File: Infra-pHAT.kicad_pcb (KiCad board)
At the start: 2 copper layers, 64 x 30 mm, 24 parts, among them Q1 BC817, U1 CAT24C32WI-GT3

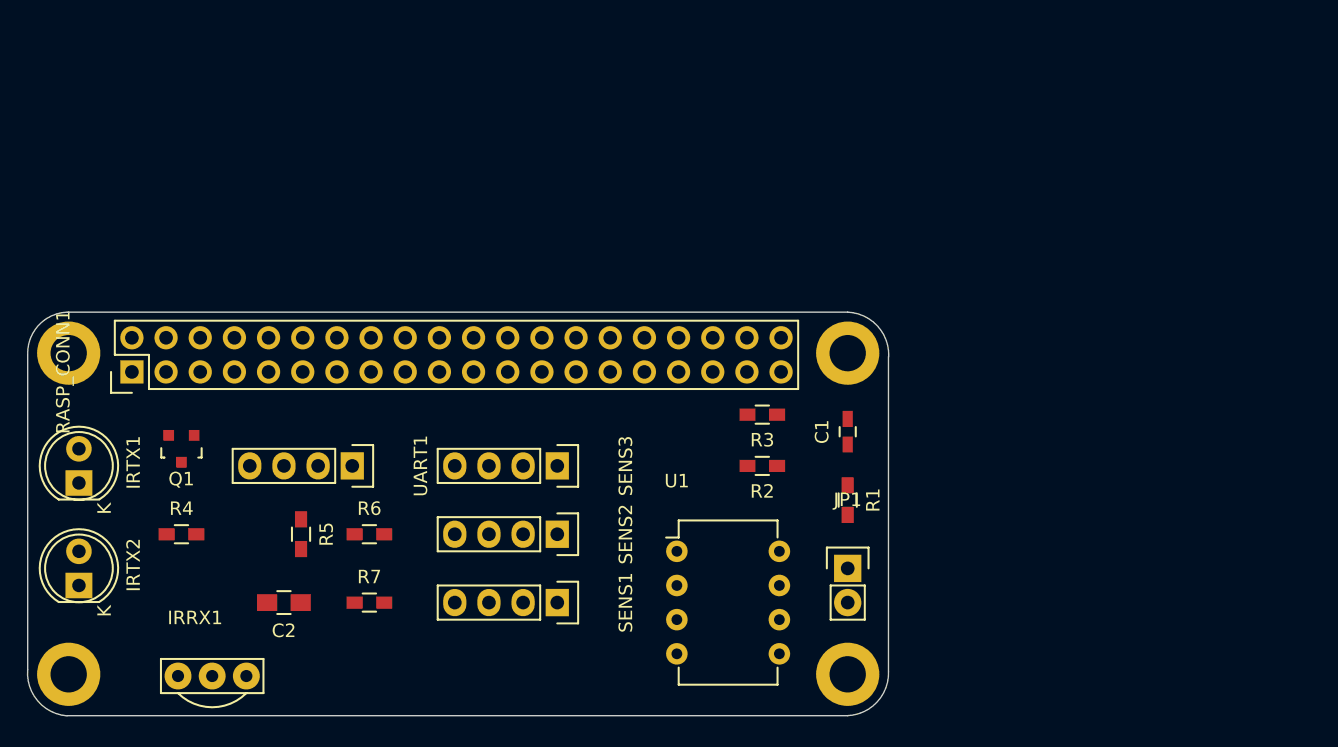
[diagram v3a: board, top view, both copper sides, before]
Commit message: Infra-pHAT.kicad_pcb: Fix edge cuts
Signed-off-by: Leon Anavi <leon@anavi.org>
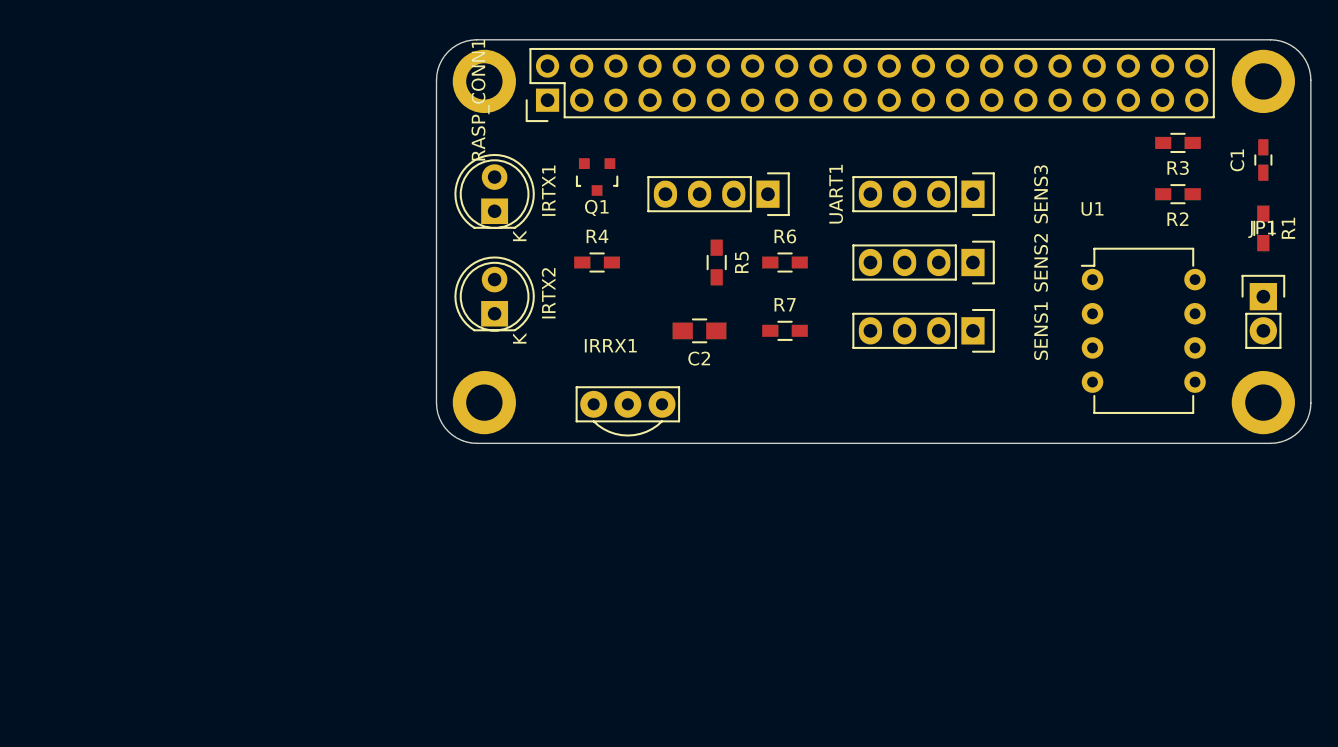
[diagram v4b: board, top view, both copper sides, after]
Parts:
- moved C1 36.9 mm to (210.0, 83.9)
- moved C2 36.9 mm to (168.1, 96.6)
- moved JP1 36.9 mm to (210.0, 94.1)
- moved Q1 36.9 mm to (160.4, 85.2)
- moved R1 36.9 mm to (210.0, 89.0)
- moved R2 36.9 mm to (203.6, 86.5)
- moved R3 36.9 mm to (203.6, 82.7)
- moved R4 36.9 mm to (160.4, 91.6)
- moved R5 36.9 mm to (169.3, 91.6)
- moved R6 36.9 mm to (174.4, 91.6)
- moved R7 36.9 mm to (174.4, 96.6)
- moved REF2 36.9 mm to (210.0, 78.1)
- moved REF3 36.9 mm to (210.0, 102.0)
- moved SENS1 36.9 mm to (188.4, 96.6)
- moved SENS2 36.9 mm to (188.4, 91.6)
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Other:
- board size 64 x 30 mm -> 65 x 30 mm
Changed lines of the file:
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@@
     (links 59)
     (no_connects 59)
-    (area 105.975429 93.919 194.252572 128.149)
+    (area 105.975429 74.953599 213.551101 126.653)
     (thickness 1.6)
-    (drawings 8)
+    (drawings 13)
     (tracks 0)
     (zones 0)
@@
   )
   (module Capacitors_SMD:C_0603_HandSoldering (layer F.Cu)
-    (at 179.07 104.14 90)
+    (at 209.97 83.94 90)
     (descr "Capacitor SMD 0603, hand soldering")
     (tags "capacitor 0603")
@@
   )
   (module Capacitors_SMD:C_0805_HandSoldering (layer F.Cu)
-    (at 137.16 116.84 180)
+    (at 168.06 96.64 180)
     (descr "Capacitor SMD 0805, hand soldering")
     (tags "capacitor 0805")
@@
   )
   (module LEDs:LED-5MM (layer F.Cu)
-    (at 121.92 107.95 90)
+    (at 152.82 87.75 90)
     (descr "LED 5mm round vertical")
     (tags "LED 5mm round vertical")
@@
   )
   (module LEDs:LED-5MM (layer F.Cu)
-    (at 121.92 115.57 90)
+    (at 152.82 95.37 90)
     (descr "LED 5mm round vertical")
     (tags "LED 5mm round vertical")
@@
   )
   (module Pin_Headers:Pin_Header_Straight_1x02 (layer F.Cu)
-    (at 179.07 114.3)
+    (at 209.97 94.1)
     (descr "Through hole pin header")
     (tags "pin header")
@@
   )
   (module TO_SOT_Packages_SMD:SOT-23 (layer F.Cu)
-    (at 129.54 105.41 180)
+    (at 160.44 85.21 180)
     (descr "SOT-23, Standard")
     (tags SOT-23)
@@
   )
   (module Resistors_SMD:R_0603_HandSoldering (layer F.Cu)
-    (at 179.07 109.22 270)
+    (at 209.97 89.02 270)
     (descr "Resistor SMD 0603, hand soldering")
     (tags "resistor 0603")
@@
   )
   (module Resistors_SMD:R_0603_HandSoldering (layer F.Cu)
-    (at 172.72 106.68 180)
+    (at 203.62 86.48 180)
     (descr "Resistor SMD 0603, hand soldering")
     (tags "resistor 0603")
@@
   )
   (module Resistors_SMD:R_0603_HandSoldering (layer F.Cu)
-    (at 172.72 102.87 180)
+    (at 203.62 82.67 180)
     (descr "Resistor SMD 0603, hand soldering")
     (tags "resistor 0603")
@@
   )
   (module Resistors_SMD:R_0603_HandSoldering (layer F.Cu)
-    (at 129.54 111.76)
+    (at 160.44 91.56)
     (descr "Resistor SMD 0603, hand soldering")
     (tags "resistor 0603")
@@
   )
   (module Resistors_SMD:R_0603_HandSoldering (layer F.Cu)
-    (at 138.43 111.76 270)
+    (at 169.33 91.56 270)
     (descr "Resistor SMD 0603, hand soldering")
     (tags "resistor 0603")
@@
   )
   (module Resistors_SMD:R_0603_HandSoldering (layer F.Cu)
-    (at 143.51 111.76)
+    (at 174.41 91.56)
     (descr "Resistor SMD 0603, hand soldering")
     (tags "resistor 0603")
@@
   )
   (module Resistors_SMD:R_0603_HandSoldering (layer F.Cu)
-    (at 143.51 116.84)
+    (at 174.41 96.64)
     (descr "Resistor SMD 0603, hand soldering")
     (tags "resistor 0603")
@@
   )
   (module Pin_Headers:Pin_Header_Straight_2x20 (layer F.Cu)
-    (at 125.857 99.695 90)
+    (at 156.757 79.495 90)
     (descr "Through hole pin header")
     (tags "pin header")
@@
   )
   (module Pin_Headers:Pin_Header_Straight_1x04 (layer F.Cu)
-    (at 157.48 116.84 270)
+    (at 188.38 96.64 270)
     (descr "Through hole pin header")
     (tags "pin header")
@@
   )
   (module Pin_Headers:Pin_Header_Straight_1x04 (layer F.Cu)
-    (at 157.48 111.76 270)
+    (at 188.38 91.56 270)
     (descr "Through hole pin header")
     (tags "pin header")
@@
   )
   (module Pin_Headers:Pin_Header_Straight_1x04 (layer F.Cu)
-    (at 157.48 106.68 270)
+    (at 188.38 86.48 270)
     (descr "Through hole pin header")
     (tags "pin header")
@@
   )
   (module Housings_DIP:DIP-8_W7.62mm (layer F.Cu)
-    (at 166.37 113.03)
+    (at 197.27 92.83)
     (descr "8-lead dip package, row spacing 7.62 mm (300 mils)")
     (tags "dil dip 2.54 300")
@@
   )
   (module Pin_Headers:Pin_Header_Straight_1x04 (layer F.Cu)
-    (at 142.24 106.68 270)
+    (at 173.14 86.48 270)
     (descr "Through hole pin header")
     (tags "pin header")
@@
   )
   (module myfootprint:TSOP38X (layer F.Cu)
-    (at 131.826 119.761)
+    (at 162.726 99.561)
     (fp_text reference IRRX1 (at -1.27 -1.778) (layer F.SilkS)
       (effects (font (size 1 1) (thickness 0.15)))
@@
   )
   (module Mounting_Holes:MountingHole_2.7mm_M2.5_DIN965_Pad (layer F.Cu)
-    (at 121.158 98.298)
+    (at 152.058 78.098)
     (descr "Mounting Hole 2.7mm, M2.5, DIN965")
     (tags "mounting hole 2.7mm m2.5 din965")
@@
   )
   (module Mounting_Holes:MountingHole_2.7mm_M2.5_DIN965_Pad (layer F.Cu)
-    (at 179.07 98.298)
+    (at 209.97 78.098)
     (descr "Mounting Hole 2.7mm, M2.5, DIN965")
     (tags "mounting hole 2.7mm m2.5 din965")
@@
   )
   (module Mounting_Holes:MountingHole_2.7mm_M2.5_DIN965_Pad (layer F.Cu)
-    (at 179.07 122.174)
+    (at 209.97 101.974)
     (descr "Mounting Hole 2.7mm, M2.5, DIN965")
     (tags "mounting hole 2.7mm m2.5 din965")
@@
   )
   (module Mounting_Holes:MountingHole_2.7mm_M2.5_DIN965_Pad (layer F.Cu)
-    (at 121.158 122.174)
+    (at 152.058 101.974)
     (descr "Mounting Hole 2.7mm, M2.5, DIN965")
     (tags "mounting hole 2.7mm m2.5 din965")
@@
     (pad 1 thru_hole circle (at 0 0) (size 4.7 4.7) (drill 2.7) (layers *.Cu *.Mask F.SilkS))
   )
-  (gr_arc (start 121.282 122.087) (end 121.028 125.262) (angle 90) (layer Edge.Cuts) (width 0.1))
-  (gr_arc (start 121.158 98.298) (end 118.11 98.425) (angle 90) (layer Edge.Cuts) (width 0.1))
-  (gr_arc (start 178.928 122.072) (end 182.103 121.945) (angle 90) (layer Edge.Cuts) (width 0.1))
-  (gr_arc (start 178.943 98.425) (end 179.07 95.25) (angle 90) (layer Edge.Cuts) (width 0.1))
-  (gr_line (start 179.07 95.25) (end 121.07 95.25) (angle 90) (layer Edge.Cuts) (width 0.1))
-  (gr_line (start 179.07 125.25) (end 121.07 125.25) (angle 90) (layer Edge.Cuts) (width 0.1))
-  (gr_line (start 118.11 98.45) (end 118.11 121.85) (angle 90) (layer Edge.Cuts) (width 0.1))
-  (gr_line (start 182.1 121.95) (end 182.1 98.55) (angle 90) (layer Edge.Cuts) (width 0.1))
+  (gr_line (start 152 78.46) (end 152 77.46) (angle 90) (layer B.SilkS) (width 0.2))
+  (gr_line (start 148.5011 102.0036) (end 148.5011 78.0036) (layer Edge.Cuts) (width 0.1))
+  (gr_line (start 210.5011 105.0036) (end 151.5011 105.0036) (layer Edge.Cuts) (width 0.1))
+  (gr_line (start 213.5011 78.0036) (end 213.5011 102.0036) (layer Edge.Cuts) (width 0.1))
+  (gr_line (start 151.5011 75.0036) (end 210.5011 75.0036) (layer Edge.Cuts) (width 0.1))
+  (gr_arc (start 151.5011 78.0036) (end 151.5011 75.0036) (angle -90) (layer Edge.Cuts) (width 0.1))
+  (gr_circle (center 152.0011 77.5036) (end 152.0011 77.5036) (layer Edge.Cuts) (width 0.1))
+  (gr_arc (start 210.5011 78.0036) (end 213.5011 78.0036) (angle -90) (layer Edge.Cuts) (width 0.1))
+  (gr_circle (center 211.0011 77.5036) (end 211.0011 77.5036) (layer Edge.Cuts) (width 0.1))
+  (gr_arc (start 210.5011 102.0036) (end 210.5011 105.0036) (angle -90) (layer Edge.Cuts) (width 0.1))
+  (gr_circle (center 211.0011 101.5036) (end 211.0011 101.5036) (layer Edge.Cuts) (width 0.1))
+  (gr_arc (start 151.5011 102.0036) (end 148.5011 102.0036) (angle -90) (layer Edge.Cuts) (width 0.1))
+  (gr_circle (center 152.0011 101.5036) (end 152.0011 101.5036) (layer Edge.Cuts) (width 0.1))
 )

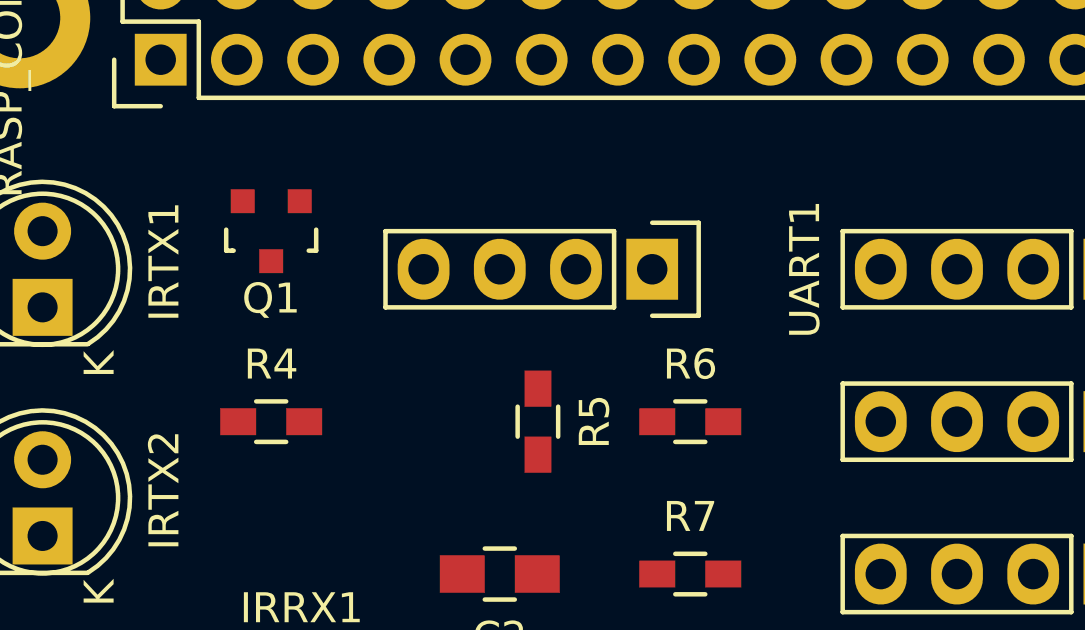
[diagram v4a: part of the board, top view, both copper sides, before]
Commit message: Infra-pHAT.kicad_pcb: make space for tracing
Signed-off-by: Leon Anavi <leon@anavi.org>
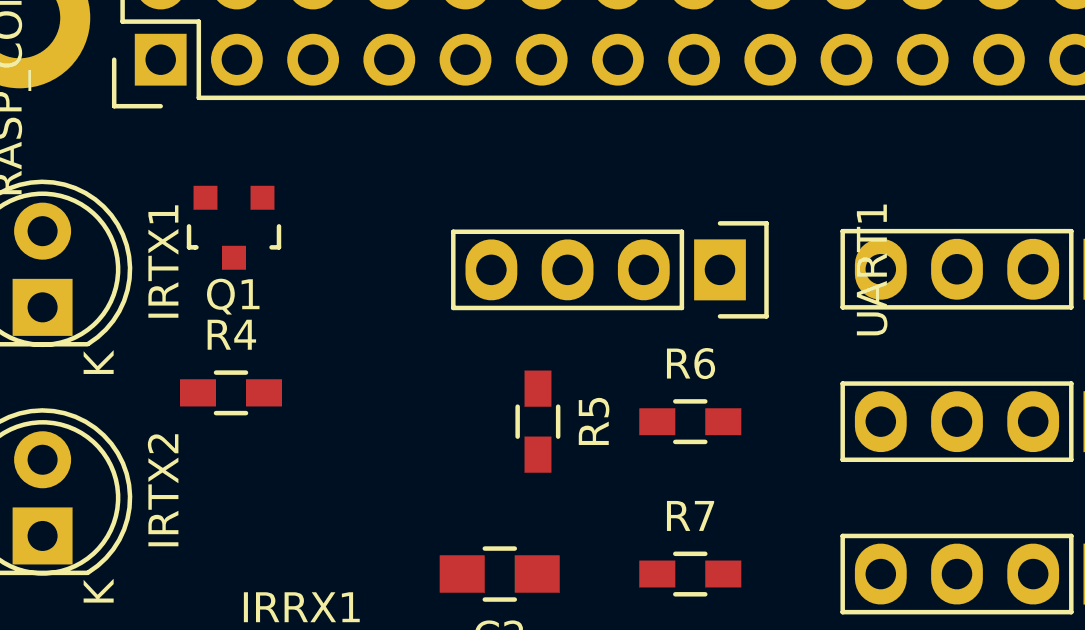
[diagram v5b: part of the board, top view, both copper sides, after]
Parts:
- moved UART1 2.26 mm to (175.4, 86.5)
- moved R4 1.65 mm to (159.1, 90.6)
- moved Q1 1.24 mm to (159.2, 85.1)
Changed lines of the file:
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@@
     (links 59)
     (no_connects 59)
-    (area 105.975429 74.953599 213.551101 126.653)
+    (area 148.451099 74.953599 213.551101 105.053601)
     (thickness 1.6)
     (drawings 13)
@@
     (pad_to_mask_clearance 0)
     (aux_axis_origin 0 0)
-    (visible_elements FFFEFFFF)
+    (visible_elements FFFCFFFF)
     (pcbplotparams
       (layerselection 0x00030_80000001)
@@
   )
   (module TO_SOT_Packages_SMD:SOT-23 (layer F.Cu)
-    (at 160.44 85.21 180)
+    (at 159.2 85.1 180)
     (descr "SOT-23, Standard")
     (tags SOT-23)
@@
   )
   (module Resistors_SMD:R_0603_HandSoldering (layer F.Cu)
-    (at 160.44 91.56)
+    (at 159.1 90.6)
     (descr "Resistor SMD 0603, hand soldering")
     (tags "resistor 0603")
@@
   )
   (module Pin_Headers:Pin_Header_Straight_1x04 (layer F.Cu)
-    (at 173.14 86.48 270)
+    (at 175.4 86.5 270)
     (descr "Through hole pin header")
     (tags "pin header")

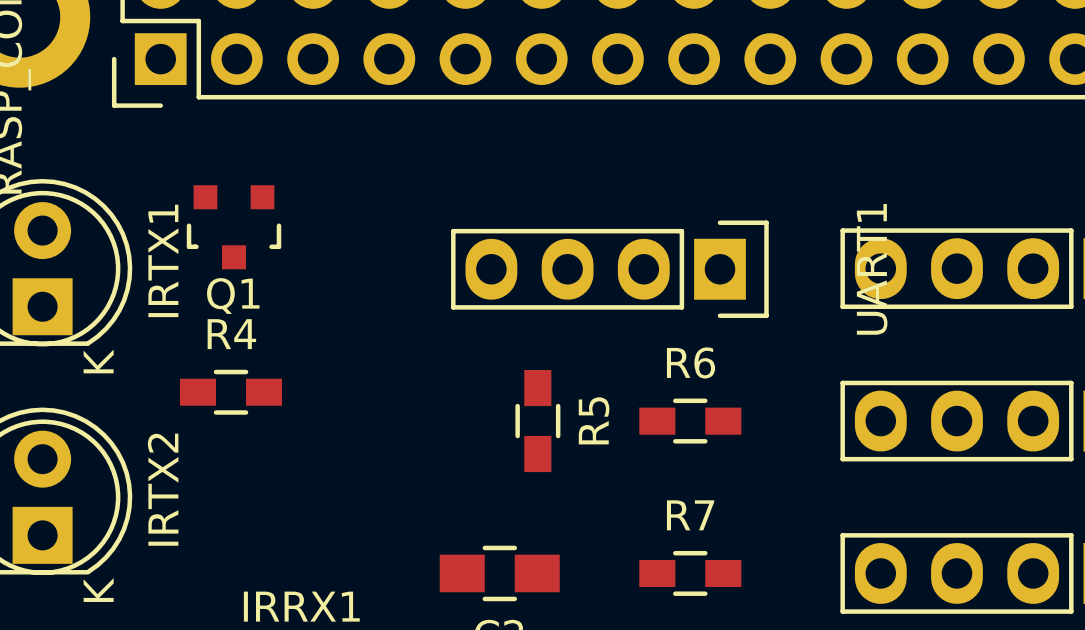
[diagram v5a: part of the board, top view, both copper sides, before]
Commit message: Infra-pHAT.kicad_pcb: Roteate UART
Signed-off-by: Leon Anavi <leon@anavi.org>
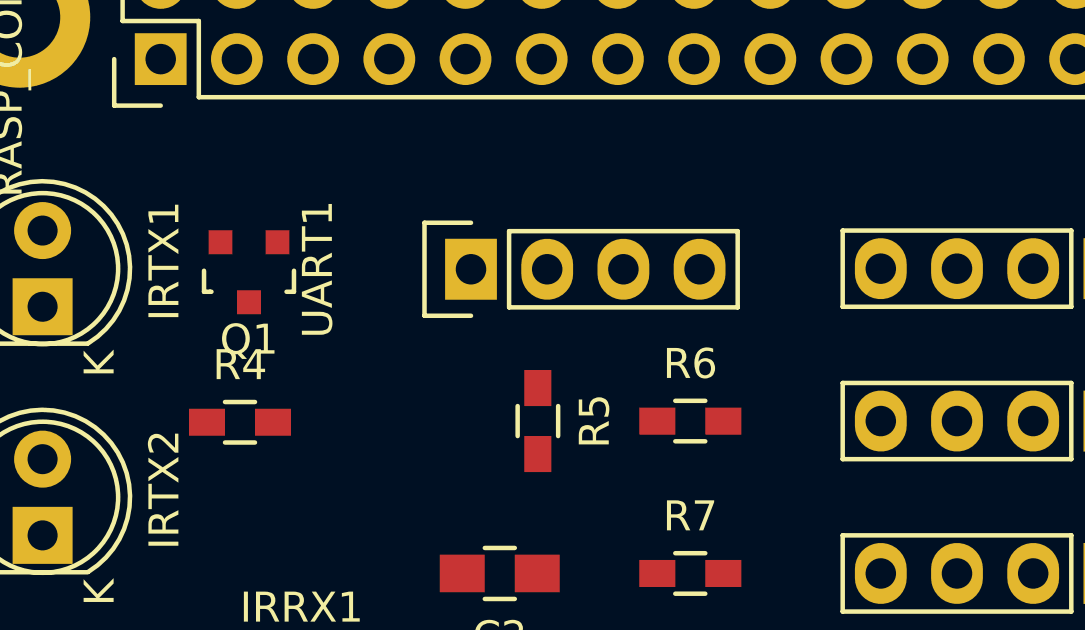
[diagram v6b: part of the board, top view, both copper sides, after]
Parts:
- moved UART1 8.30 mm to (167.1, 86.5), turned to 90 degrees
- moved Q1 1.58 mm to (159.7, 86.6)
- moved R4 1.04 mm to (159.4, 91.6)
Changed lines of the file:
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@@
     (links 59)
     (no_connects 59)
-    (area 148.451099 74.953599 213.551101 105.053601)
+    (area 136.875429 73.719 225.152572 106.453)
     (thickness 1.6)
     (drawings 13)
@@
   )
   (module TO_SOT_Packages_SMD:SOT-23 (layer F.Cu)
-    (at 159.2 85.1 180)
+    (at 159.7 86.6 180)
     (descr "SOT-23, Standard")
     (tags SOT-23)
@@
   )
   (module Resistors_SMD:R_0603_HandSoldering (layer F.Cu)
-    (at 159.1 90.6)
+    (at 159.4 91.6)
     (descr "Resistor SMD 0603, hand soldering")
     (tags "resistor 0603")
@@
   )
   (module Pin_Headers:Pin_Header_Straight_1x04 (layer F.Cu)
-    (at 175.4 86.5 270)
+    (at 167.1 86.5 90)
     (descr "Through hole pin header")
     (tags "pin header")
-    (fp_text reference UART1 (at 0 -5.1 270) (layer F.SilkS)
-      (effects (font (size 1 1) (thickness 0.15)))
-    )
-    (fp_text value CONN_01X04 (at 0 -3.1 270) (layer F.Fab)
+    (fp_text reference UART1 (at 0 -5.1 90) (layer F.SilkS)
+      (effects (font (size 1 1) (thickness 0.15)))
+    )
+    (fp_text value CONN_01X04 (at 0 -3.1 90) (layer F.Fab)
       (effects (font (size 1 1) (thickness 0.15)))
     )
@@
     (fp_line (start -1.55 0) (end -1.55 -1.55) (layer F.SilkS) (width 0.15))
     (fp_line (start -1.55 -1.55) (end 1.55 -1.55) (layer F.SilkS) (width 0.15))
-    (pad 1 thru_hole rect (at 0 0 270) (size 2.032 1.7272) (drill 1.016) (layers *.Cu *.Mask F.SilkS)
-      (net 1 +3V3))
-    (pad 2 thru_hole oval (at 0 2.54 270) (size 2.032 1.7272) (drill 1.016) (layers *.Cu *.Mask F.SilkS)
+    (pad 1 thru_hole rect (at 0 0 90) (size 2.032 1.7272) (drill 1.016) (layers *.Cu *.Mask F.SilkS)
+      (net 1 +3V3))
+    (pad 2 thru_hole oval (at 0 2.54 90) (size 2.032 1.7272) (drill 1.016) (layers *.Cu *.Mask F.SilkS)
       (net 12 /TXD))
-    (pad 3 thru_hole oval (at 0 5.08 270) (size 2.032 1.7272) (drill 1.016) (layers *.Cu *.Mask F.SilkS)
+    (pad 3 thru_hole oval (at 0 5.08 90) (size 2.032 1.7272) (drill 1.016) (layers *.Cu *.Mask F.SilkS)
       (net 13 /RXD))
-    (pad 4 thru_hole oval (at 0 7.62 270) (size 2.032 1.7272) (drill 1.016) (layers *.Cu *.Mask F.SilkS)
+    (pad 4 thru_hole oval (at 0 7.62 90) (size 2.032 1.7272) (drill 1.016) (layers *.Cu *.Mask F.SilkS)
       (net 2 GND))
     (model Pin_Headers.3dshapes/Pin_Header_Straight_1x04.wrl
